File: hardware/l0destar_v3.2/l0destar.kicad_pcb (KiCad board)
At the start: 4 copper layers, 66.7 x 37.5 mm, 155 parts

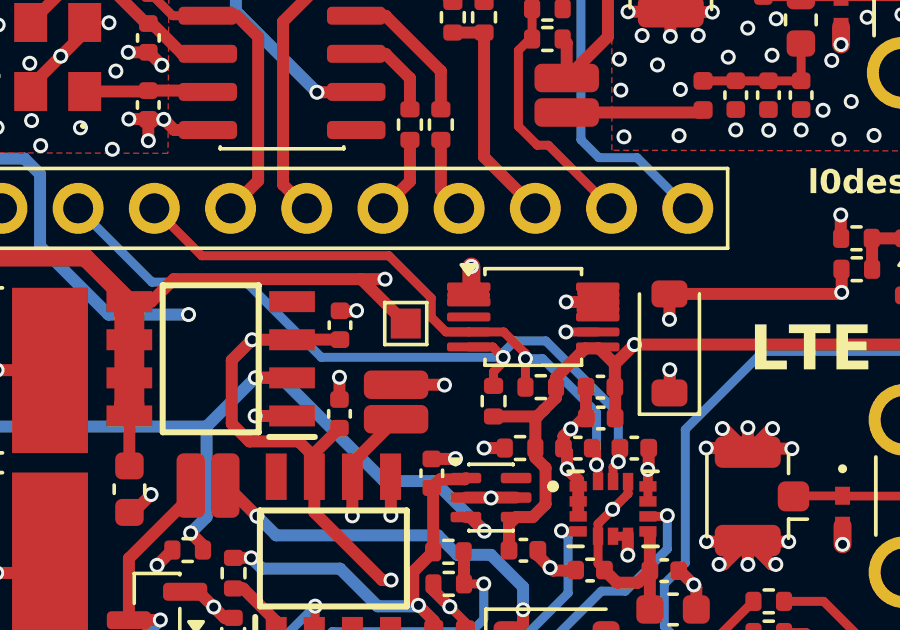
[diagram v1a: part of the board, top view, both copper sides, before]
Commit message: spec anti-sulfur for S6R3
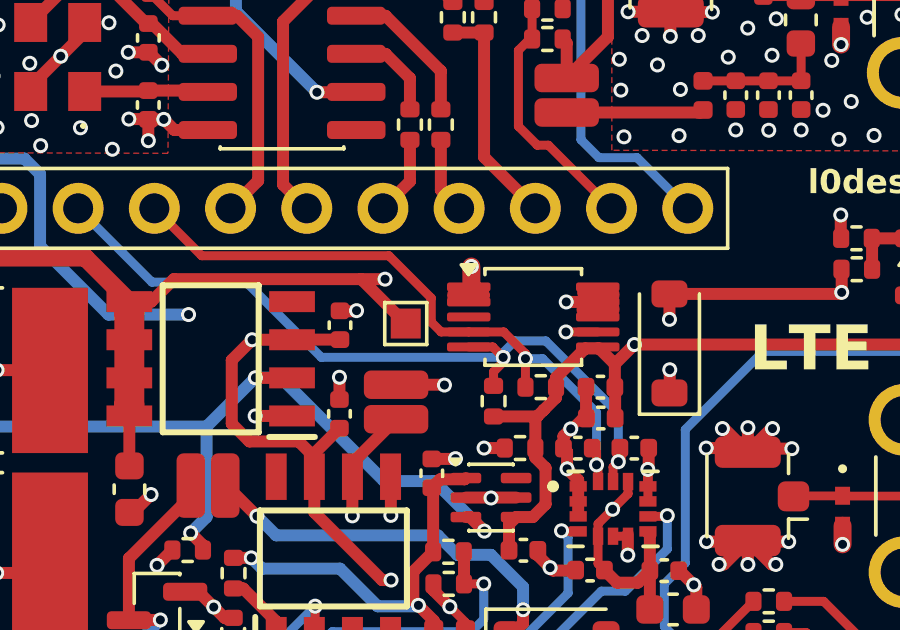
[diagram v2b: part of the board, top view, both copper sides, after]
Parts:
- S6R3: value 0402 1M 1% -> 0402 1M 1% ANTI-SULFUR AEC-Q200
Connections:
- S3U1 pad 3: INA_ALRT -> unconnected-(S3U1-~{Alert}-Pad3)
